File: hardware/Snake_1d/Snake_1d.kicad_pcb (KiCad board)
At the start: 2 copper layers, 60 x 60 mm, 21 parts, among them J1 LED_strip_connector, J2 SPI, Q1 PMN48XP, SW1 SW_Push, U1 SN74LVC1G14DBV, U2 ATtiny85-20SU

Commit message: Adds revision number to silkscreen on pcb
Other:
- board text added: "rev 0.1"

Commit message: Adds pin 1 marks to ICs on the PCB
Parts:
- added Ref**: Val**, Amieiro:Pin1_FSilks, F.Cu at (159.5, 80.0)
- added Ref**: Val**, Amieiro:Pin1_FSilks, F.Cu at (136.5, 92.8)
- added Ref**: Val**, Amieiro:Pin1_FSilks, F.Cu at (137.5, 81.8)

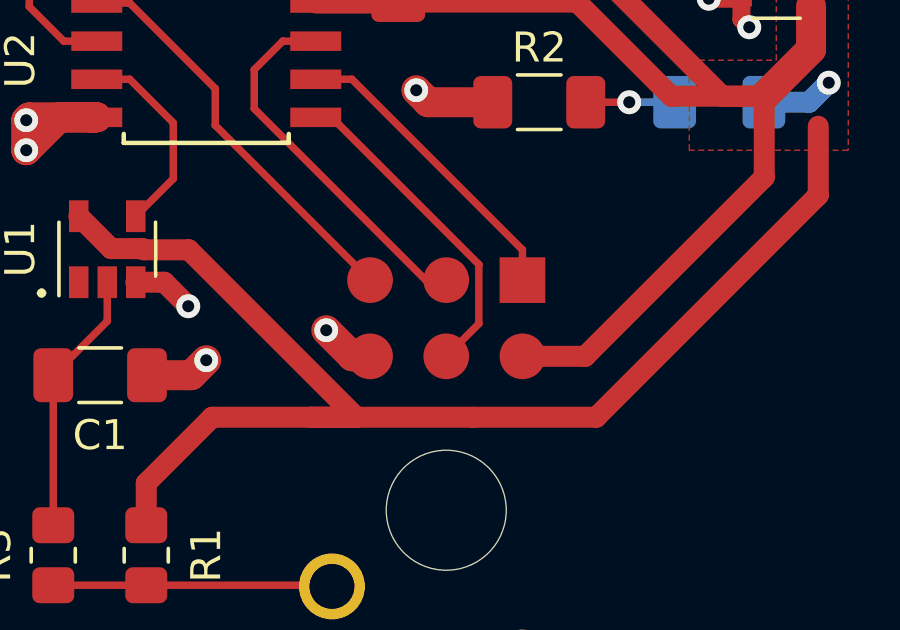
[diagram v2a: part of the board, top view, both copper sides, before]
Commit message: Adds silkscreen labels to programming connector on PCB
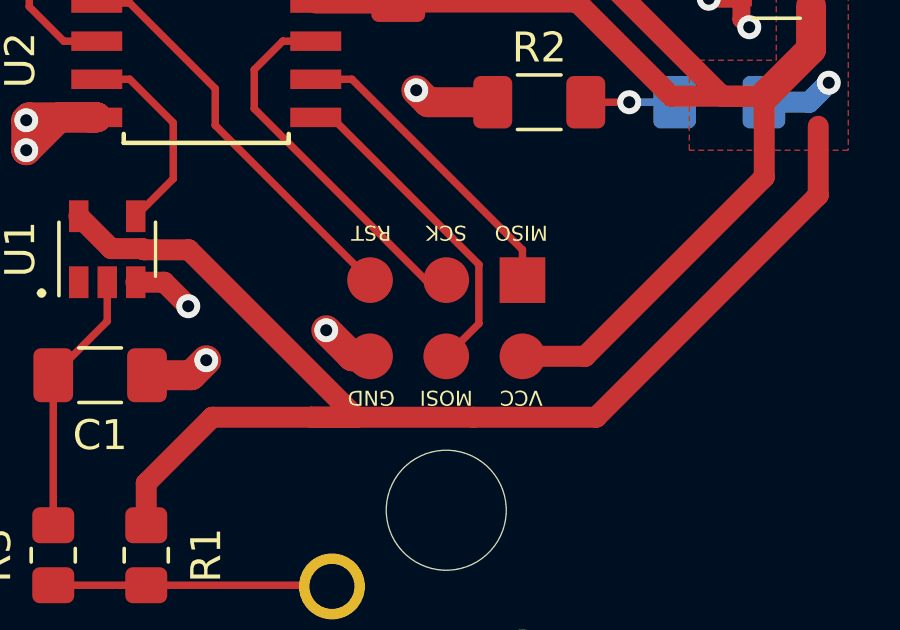
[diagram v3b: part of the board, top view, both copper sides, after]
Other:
- board text added: "GND"
- board text added: "MISO"
- board text added: "MOSI"
- board text added: "RST"
- board text added: "SCK"
- board text added: "VCC"
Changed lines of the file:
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@@
   (general
     (thickness 1.6)
-    (drawings 3)
+    (drawings 9)
     (tracks 108)
     (zones 0)
@@
     )
   )
+  (gr_text RST (at 147.5 90.75 180) (layer F.SilkS)
+    (effects (font (size 0.5 0.5) (thickness 0.125)))
+  )
+  (gr_text SCK (at 150 90.75 180) (layer F.SilkS)
+    (effects (font (size 0.5 0.5) (thickness 0.125)))
+  )
+  (gr_text MISO (at 152.5 90.75 180) (layer F.SilkS)
+    (effects (font (size 0.5 0.5) (thickness 0.125)))
+  )
+  (gr_text VCC (at 152.5 96.25 180) (layer F.SilkS)
+    (effects (font (size 0.5 0.5) (thickness 0.125)))
+  )
+  (gr_text MOSI (at 150 96.25 180) (layer F.SilkS)
+    (effects (font (size 0.5 0.5) (thickness 0.125)))
+  )
+  (gr_text GND (at 147.5 96.25 180) (layer F.SilkS)
+    (effects (font (size 0.5 0.5) (thickness 0.125)))
+  )
   (gr_text "rev 0.1" (at 175 95.25) (layer F.SilkS)

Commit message: Adds JLC order number placeholder to pcb
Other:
- board text added: "JLCJLCJLCJLC"
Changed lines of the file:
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@@
   (general
     (thickness 1.6)
-    (drawings 9)
+    (drawings 10)
     (tracks 108)
     (zones 0)
@@
     )
   )
+  (gr_text JLCJLCJLCJLC (at 149.86 95.758) (layer B.SilkS)
+    (effects (font (size 1 1) (thickness 0.25)) (justify mirror))
+  )
   (gr_text RST (at 147.5 90.75 180) (layer F.SilkS)

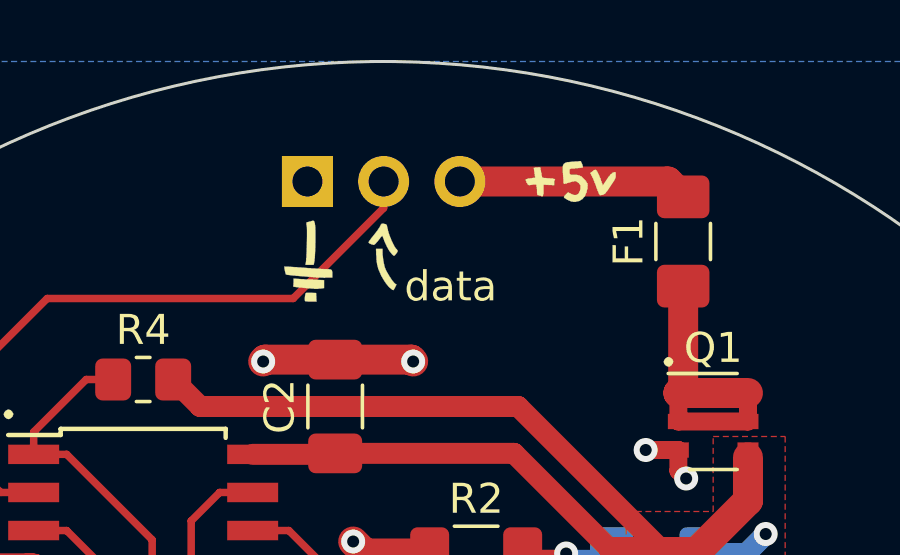
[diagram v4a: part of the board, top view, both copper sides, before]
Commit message: Moves connector label to the front side of the PCB
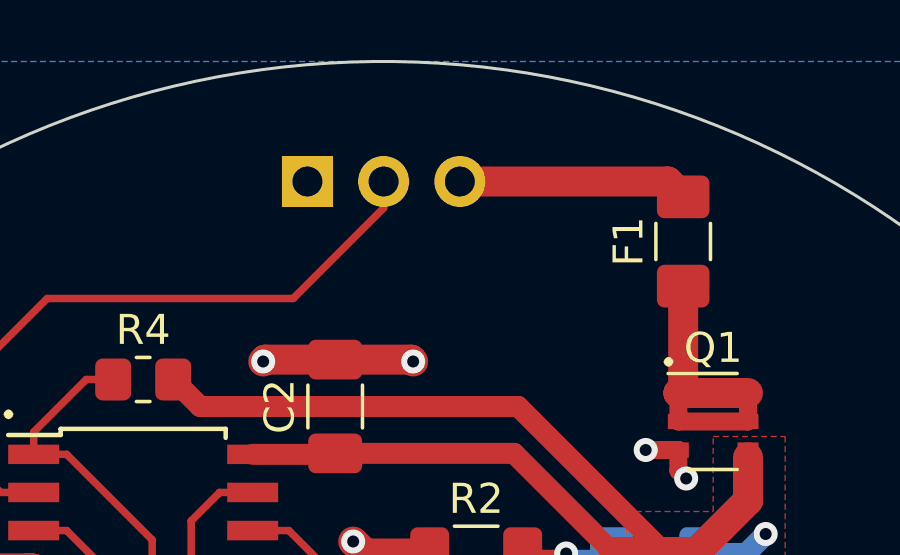
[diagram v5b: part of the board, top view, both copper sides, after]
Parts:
- Ref** (x3): moved to B.Cu
- turned Ref** to 180 degrees (x3)

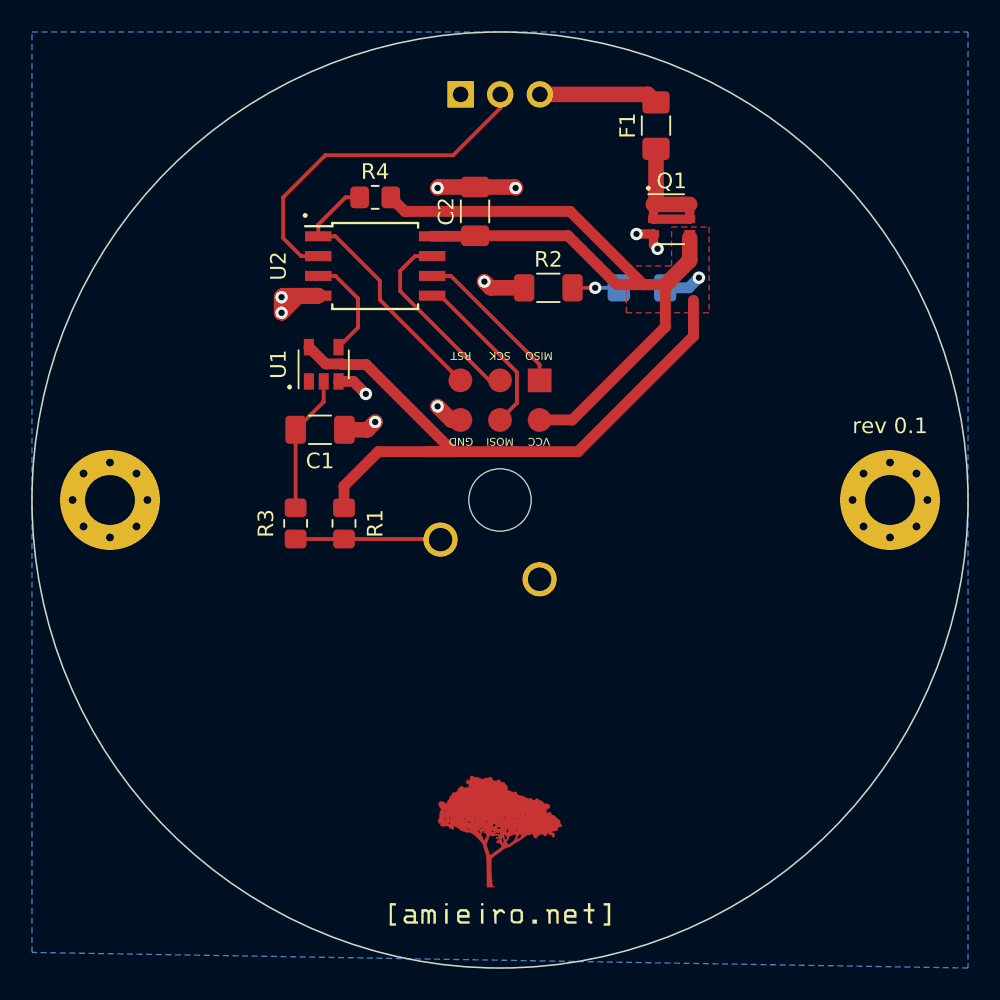
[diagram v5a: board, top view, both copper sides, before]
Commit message: Changes cherry switch to PCB mount
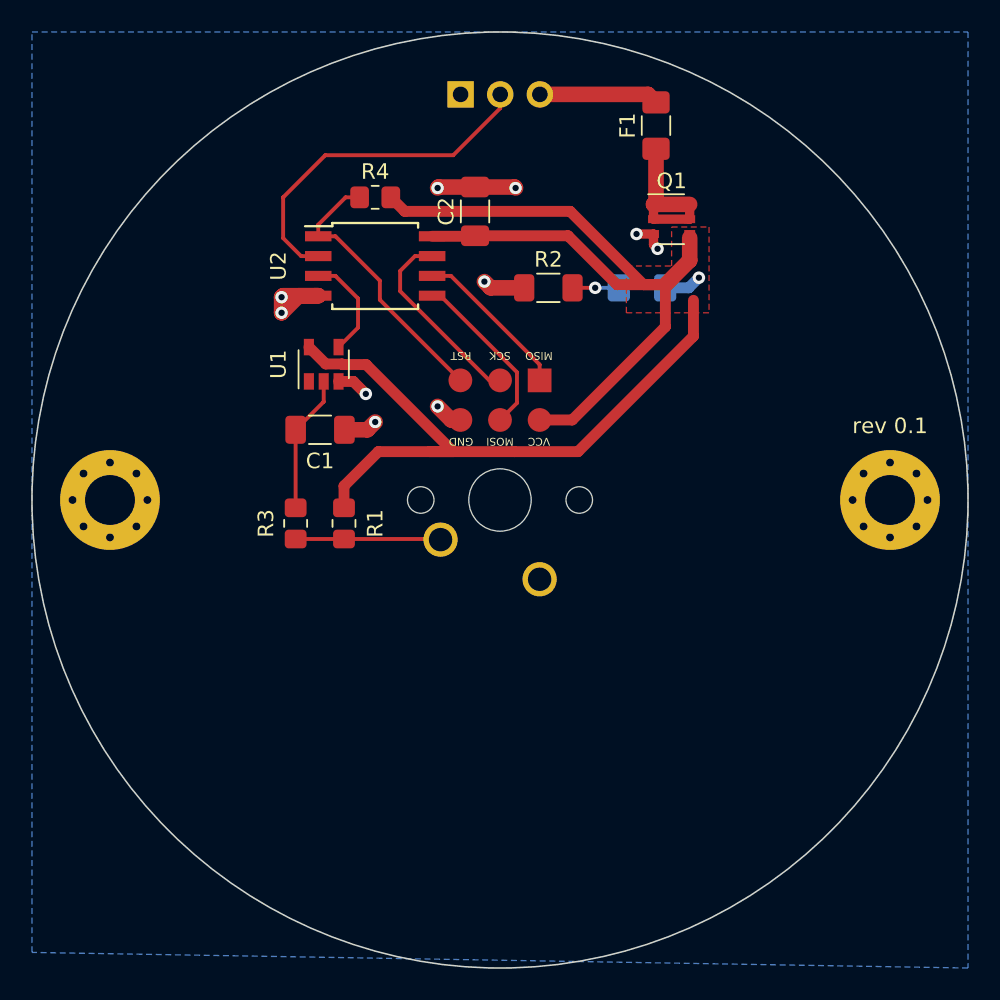
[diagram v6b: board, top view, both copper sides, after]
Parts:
- removed Ref** (x3): Val**, Amieiro:Pin1_FSilks
- removed Ref**: Val**, Amieiro:url_bsilks
- removed Ref**: Val**, Amieiro:ipe_logo
- removed Ref**: Val**, Amieiro:5v_FSilks
- removed Ref**: Val**, Amieiro:arrow
- removed Ref**: Val**, Amieiro:ground_FSilks
- SW1: footprint Button_Switch_Keyboard:SW_Cherry_MX_1.00u_Plate -> Button_Switch_Keyboard:SW_Cherry_MX_1.00u_PCB

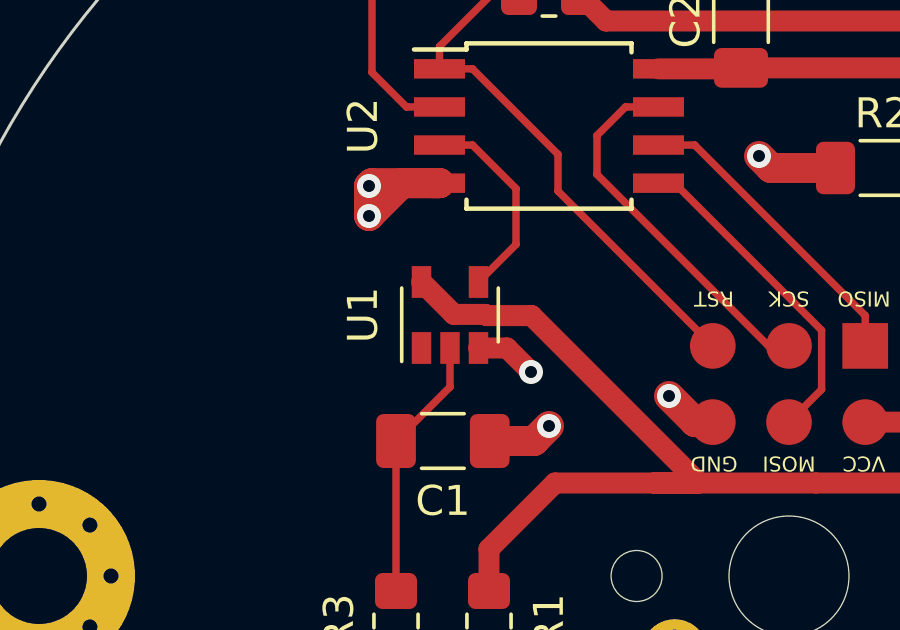
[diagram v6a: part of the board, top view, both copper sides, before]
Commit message: Changes footprints to handsolder where possible
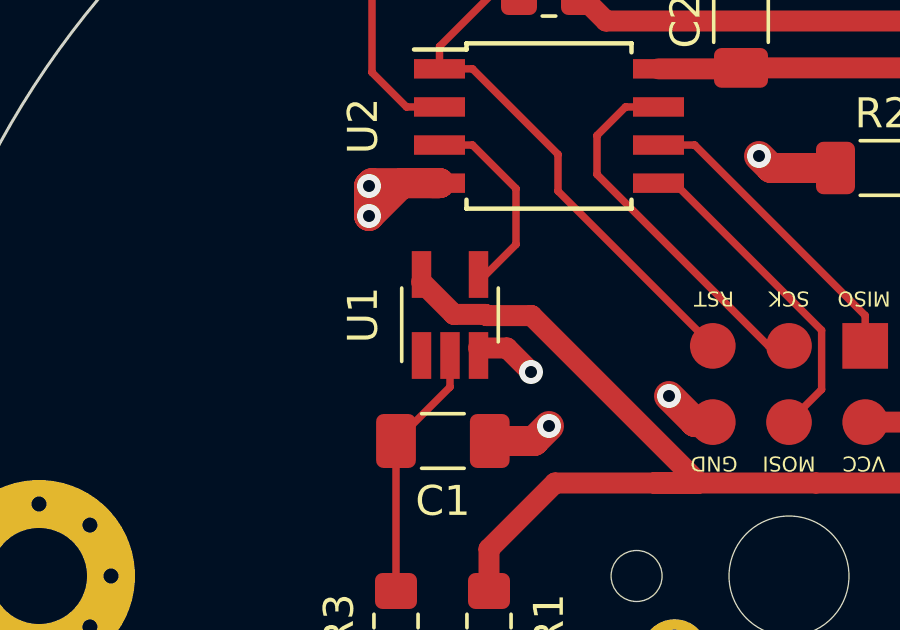
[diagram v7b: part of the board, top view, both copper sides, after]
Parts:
- U1: footprint Package_TO_SOT_SMD:SOT-23-5 -> Package_TO_SOT_SMD:SOT-23-5_HandSoldering
